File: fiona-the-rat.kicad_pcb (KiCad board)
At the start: 2 copper layers, 83.3 x 89.9 mm, 104 parts, among them J1 USB_TP_P, J10 ~{CHG}_TP, J11 +1V1_TP, J12 VBAT_TP, J13 +3V3_TP, J14 SWD, J15 BMS_COUT_TP, J16 BMS_DOUT_TP, J17 BAT_P_JMP, J18 BAT_N_JMP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

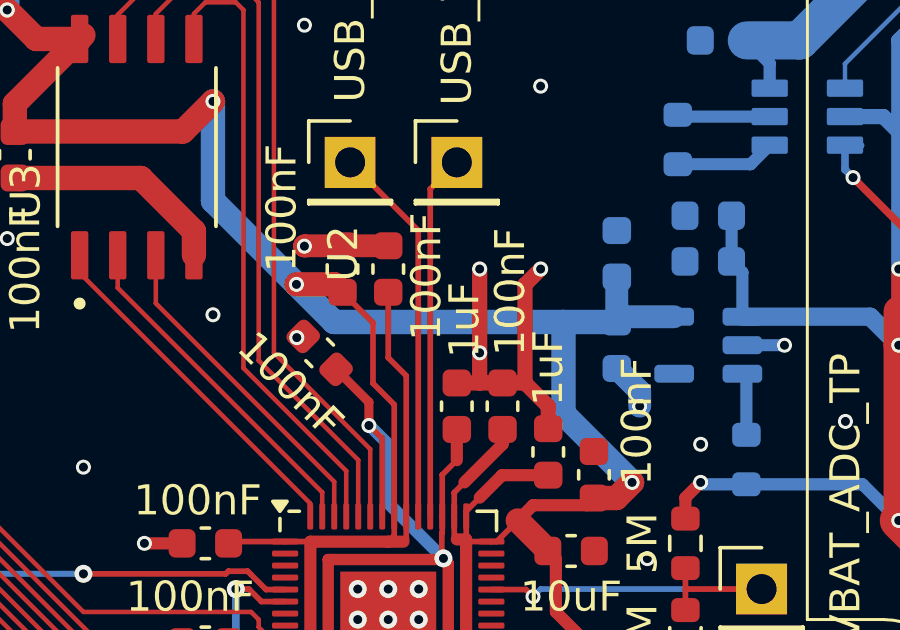
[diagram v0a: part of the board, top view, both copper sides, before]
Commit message: swap 3v3 caps on rp2040
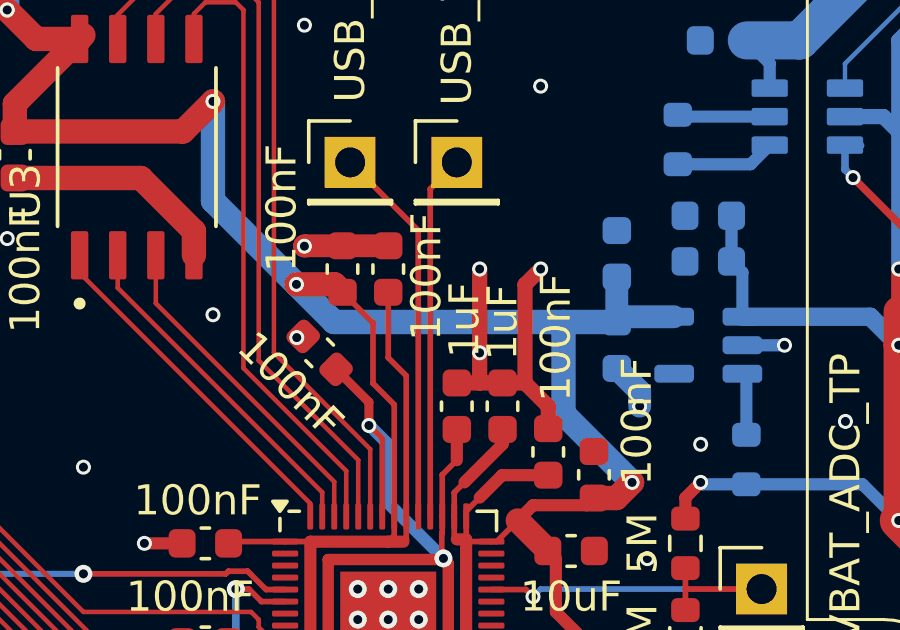
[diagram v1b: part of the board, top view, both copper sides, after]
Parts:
- moved C11 2.16 mm to (143.5, 94.5)
- moved C22 2.16 mm to (145.0, 96.0)
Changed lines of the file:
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@@
 	(footprint "Capacitor_SMD:C_0603_1608Metric"
 		(layer "F.Cu")
-		(at 143.51 94.488 90)
+		(at 145.034 96.012 90)
 		(descr "Capacitor SMD 0603 (1608 Metric), square (rectangular) end terminal, IPC-7351 nominal, (Body size source: IPC-SM-782 page 76, https://www.pcb-3d.com/wordpress/wp-content/uploads/ipc-sm-782a_amendment_1_and_2.pdf), generated with kicad-footprint-generator")
 		(tags "capacitor")
@@
 		(at 139.7 88.9 90)
 		(property "Reference" "U2"
-			(at -0.5 -1.5 90)
+			(at 0.008 3.072 90)
 			(unlocked yes)
 			(layer "F.SilkS")
+			(hide yes)
 			(effects
 				(font
@@
 			(layer "F.SilkS")
 		)
-		(fp_text user "${REFERENCE}"
-			(at -0.5 1.5 90)
-			(unlocked yes)
-			(layer "F.Fab")
-			(effects
-				(font
-					(size 1 1)
-					(thickness 0.15)
-				)
-			)
-		)
 		(pad "1" thru_hole circle
 			(at 15.237545 -12.7 90)
@@
 				"a2ccb8ad-579d-4426-9feb-ad976e31a146" "a3a729a7-c3e8-4f9c-9854-a2e688bbd4e9"
 				"acdef2fa-4fc8-4049-8d66-e1936bda30b8" "ce06db57-7f60-4f2b-af29-020d9ed6190e"
-				"ce06db57-7f60-4f2b-af29-020d9ed6190e" "ce06db57-7f60-4f2b-af29-020d9ed6190e"
-				"ce06db57-7f60-4f2b-af29-020d9ed6190e" "ce18d080-f9fe-4c4e-bd94-48005d2792bd"
-				"d182e725-c283-4e68-ab7d-6e44680550b5" "e2b29b8d-fd9e-490c-9fd3-35cf895c7c33"
-				"f8c461c9-510e-430b-a64b-ff15fdf24184"
+				"ce18d080-f9fe-4c4e-bd94-48005d2792bd" "d182e725-c283-4e68-ab7d-6e44680550b5"
+				"e2b29b8d-fd9e-490c-9fd3-35cf895c7c33" "f8c461c9-510e-430b-a64b-ff15fdf24184"
 			)
 		)
@@
 	(footprint "Capacitor_SMD:C_0603_1608Metric"
 		(layer "F.Cu")
-		(at 145.034 96.012 90)
+		(at 143.51 94.488 90)
 		(descr "Capacitor SMD 0603 (1608 Metric), square (rectangular) end terminal, IPC-7351 nominal, (Body size source: IPC-SM-782 page 76, https://www.pcb-3d.com/wordpress/wp-content/uploads/ipc-sm-782a_amendment_1_and_2.pdf), generated with kicad-footprint-generator")
 		(tags "capacitor")
@@
 	)
 	(segment
-		(start 142.3 97.984)
-		(end 142.748 97.536)
-		(width 0.1905)
-		(layer "F.Cu")
-		(net 3)
-	)
-	(segment
 		(start 137.1 99)
 		(end 137.1042 99.0042)
@@
 	)
 	(segment
+		(start 142.3 98.9238)
+		(end 142.2958 98.928)
+		(width 0.1905)
+		(layer "F.Cu")
+		(net 3)
+	)
+	(segment
 		(start 128.765 70.117)
 		(end 128.765 70.104)
@@
 	)
 	(segment
-		(start 142.3 98.1625)
-		(end 142.3 98.9238)
-		(width 0.1905)
-		(layer "F.Cu")
-		(net 3)
-	)
-	(segment
 		(start 127.967 82.247)
 		(end 127 81.28)
@@
 	)
 	(segment
-		(start 142.3 98.1625)
-		(end 142.3 97.984)
-		(width 0.1905)
-		(layer "F.Cu")
-		(net 3)
-	)
-	(segment
 		(start 140.3 98.1625)
 		(end 140.3 93.472)
@@
 	)
 	(segment
-		(start 142.3 98.9238)
-		(end 142.2958 98.928)
-		(width 0.1905)
-		(layer "F.Cu")
-		(net 3)
-	)
-	(segment
 		(start 127.254 85.331)
 		(end 127.254 84.406)
@@
 	)
 	(segment
+		(start 142.3 97.984)
+		(end 142.748 97.536)
+		(width 0.1905)
+		(layer "F.Cu")
+		(net 3)
+	)
+	(segment
+		(start 142.3 98.1625)
+		(end 142.3 97.984)
+		(width 0.1905)
+		(layer "F.Cu")
+		(net 3)
+	)
+	(segment
 		(start 139.970042 104.394)
 		(end 140.092042 104.272)
@@
 		(layer "F.Cu")
 		(net 3)
+	)
+	(segment
+		(start 142.3 98.1625)
+		(end 142.3 98.9238)
+		(width 0.1905)
+		(layer "F.Cu")
+		(net 3)

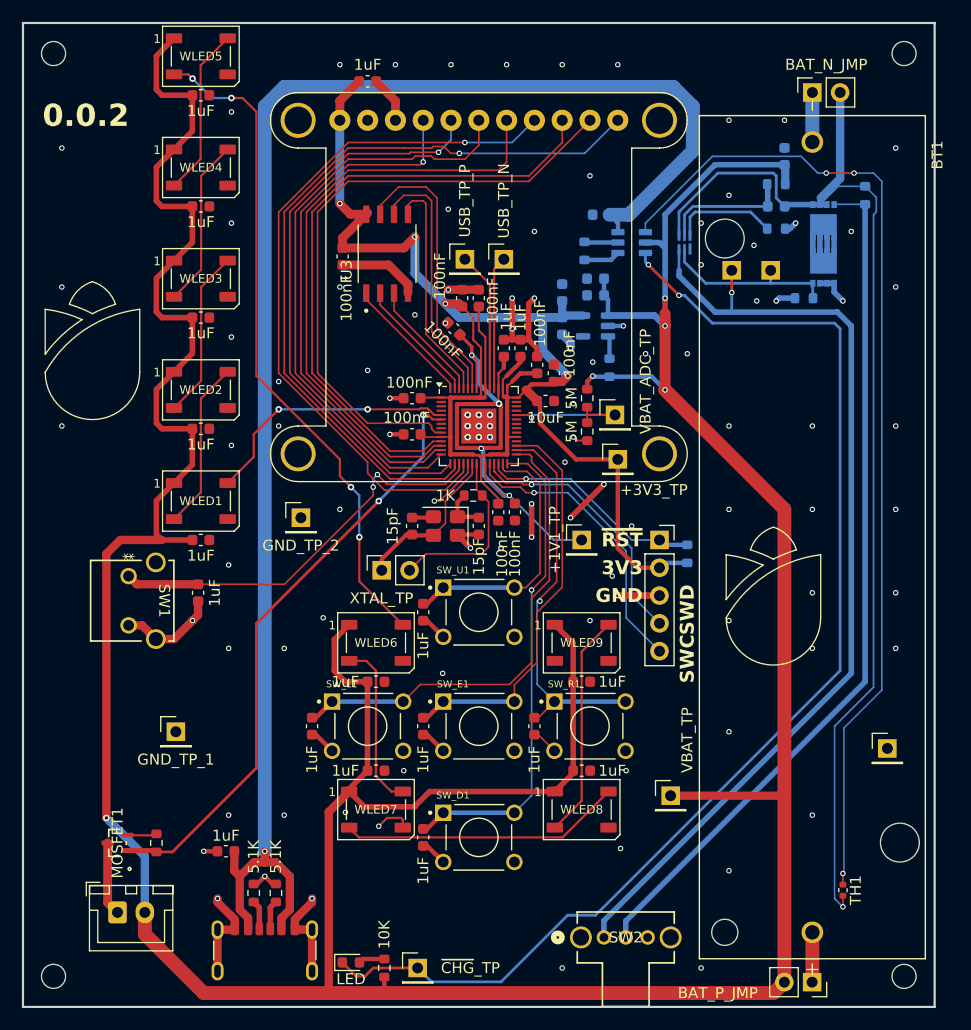
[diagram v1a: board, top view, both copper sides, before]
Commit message: breakout GPIO[0..=2]
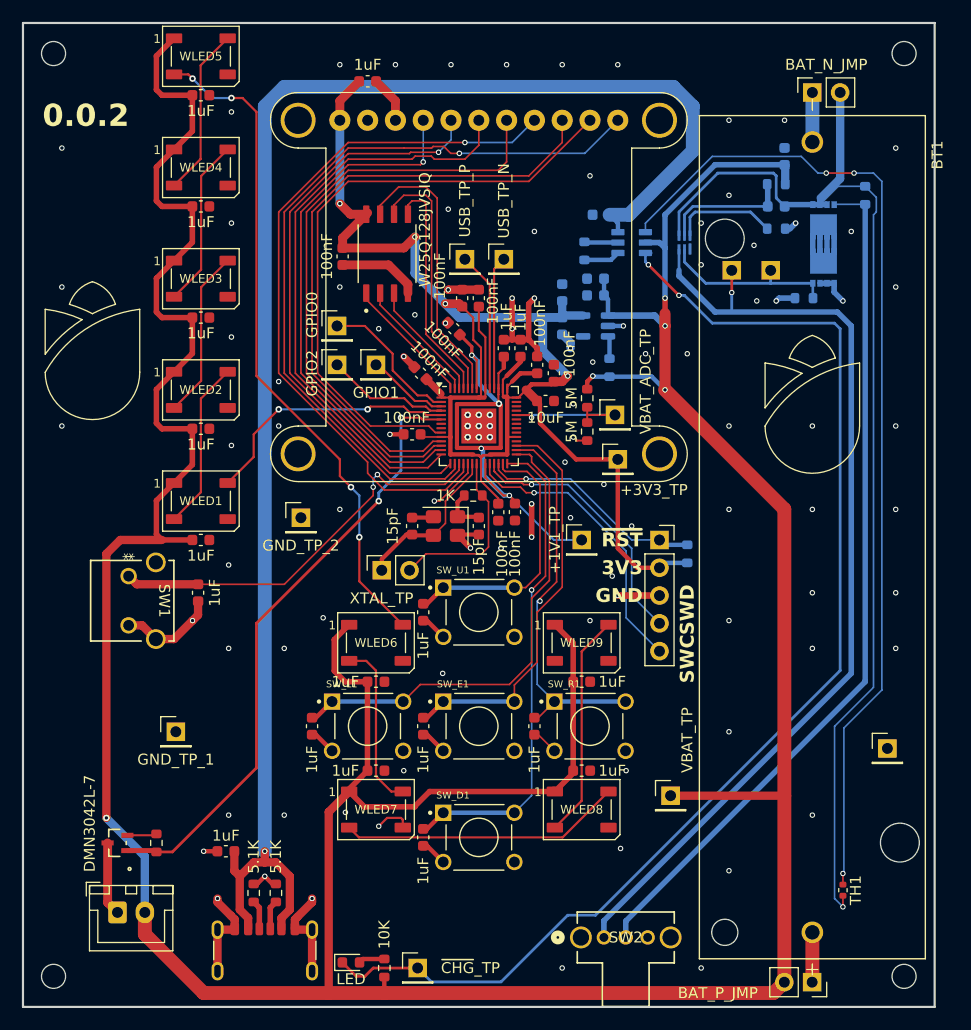
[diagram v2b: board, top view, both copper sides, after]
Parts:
- added J19: GPIO0, Connector_PinHeader_2.54mm:PinHeader_1x01_P2.54mm_Vertical, F.Cu at (126.7, 92.5)
- added J20: GPIO1, Connector_PinHeader_2.54mm:PinHeader_1x01_P2.54mm_Vertical, F.Cu at (130.3, 96.0)
- added J21: GPIO2, Connector_PinHeader_2.54mm:PinHeader_1x01_P2.54mm_Vertical, F.Cu at (126.7, 96.0)
- moved C23 2.41 mm to (134.4, 96.8), turned to 135 degrees
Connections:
- U1 pad 2: unconnected-(U1-GPIO0-Pad2) -> Net-(J19-Pin_1)
- U1 pad 3: unconnected-(U1-GPIO1-Pad3) -> Net-(J20-Pin_1)
- U1 pad 4: unconnected-(U1-GPIO2-Pad4) -> Net-(J21-Pin_1)
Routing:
- net Net-(J19-Pin_1): track 0.00 -> 13.3 mm
- net Net-(J21-Pin_1): track 0.00 -> 11.6 mm
- net Net-(J20-Pin_1): track 0.00 -> 7.53 mm
- net GND: track 125.7 -> 121.5 mm
- net Net-(MOSFET1-G): track 55.4 -> 56.2 mm

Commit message: add haptic motor
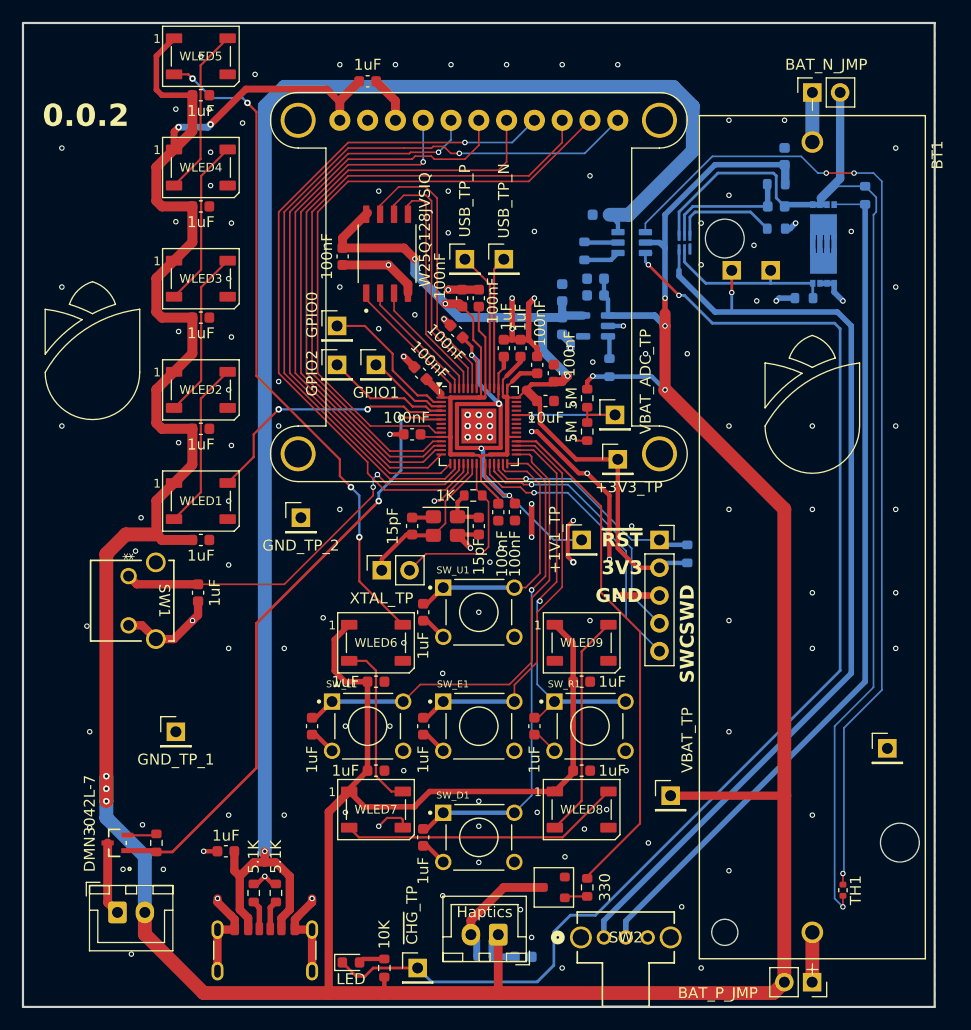
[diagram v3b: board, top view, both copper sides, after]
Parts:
- removed REF** (x4): MountingHole_2.2mm_M2, MountingHole:MountingHole_2.2mm_M2
- added C40: 10uF, Capacitor_SMD:C_0603_1608Metric, B.Cu at (143.8, 150.1)
- added D2: 1N4148WT, Diode_SMD:D_SOD-523, B.Cu at (140.2, 150.1)
- added J22: Haptics, Connector_JST:JST_XH_B2B-XH-A_1x02_P2.50mm_Vertical, F.Cu at (141.5, 148.1)
- added Q1: MMBT2222A, PCM_Package_TO_SOT_SMD_AKL:SOT-23, F.Cu at (146.6, 143.8)
- added R15: 330, Resistor_SMD:R_0603_1608Metric, F.Cu at (149.6, 143.8)
- moved C8 0.36 mm to (137.7, 93.0)
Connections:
- C2 pad 1: +3V3 -> VBAT
- U1 pad 32: unconnected-(U1-GPIO21-Pad32) -> Net-(U1-GPIO21)
- U2 pad 1: +3V3 -> VBAT
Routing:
- net Net-(U1-GPIO21): track 0.00 -> 47.7 mm
- net VBAT: track 365.5 -> 402.0 mm, vias 5 -> 9
- net GND: track 121.5 -> 141.7 mm, vias 103 -> 144
- net +3V3: track 147.3 -> 130.6 mm, vias 4 -> 3
- net Net-(D2-A): track 0.00 -> 11.4 mm
- net Net-(Q1-B): track 0.00 -> 2.10 mm
- net ~{CHG}: track 111.0 -> 112.8 mm

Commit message: Flipped display pin ordering
:/
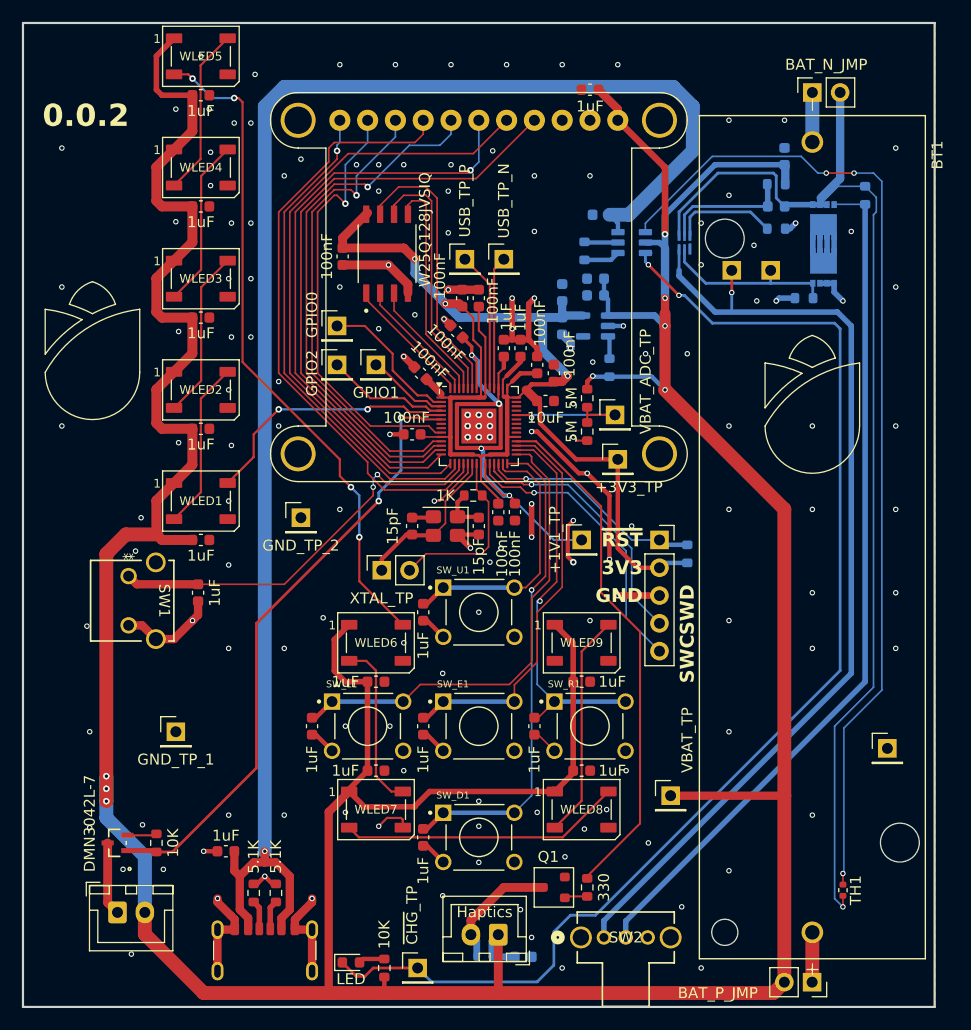
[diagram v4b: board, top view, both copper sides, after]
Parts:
- moved C2 20.3 mm to (149.9, 70.9), turned to 180 degrees
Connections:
- U2 pad 1: VBAT -> BACKLIGHT
- U2 pad 10: SD_CS -> unconnected-(U2-+3V3-Pad10)
- U2 pad 11: BACKLIGHT -> VBAT
- U2 pad 2: unconnected-(U2-+3V3-Pad2) -> SD_CS
- U2 pad 3: GND -> LCD_DCX
- U2 pad 4: LCD_CLK -> LCD_RST
- U2 pad 5: LCD_MISO -> LCD_CS
- U2 pad 7: LCD_CS -> LCD_MISO
- U2 pad 8: LCD_RST -> LCD_CLK
- U2 pad 9: LCD_DCX -> GND
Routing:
- net BACKLIGHT: track 69.7 -> 45.7 mm
- net SD_CS: track 56.6 -> 40.2 mm, vias 0 -> 1
- net LCD_DCX: track 57.4 -> 43.3 mm, vias 0 -> 1
- net VBAT: track 402.0 -> 392.9 mm, vias 9 -> 8
- net LCD_RST: track 64.9 -> 56.2 mm, vias 1 -> 0
- net LCD_CLK: track 48.3 -> 56.2 mm, vias 1 -> 0
- net LCD_CS: track 54.6 -> 48.2 mm, vias 0 -> 1
- net GND: track 141.7 -> 137.4 mm, vias 144 -> 156
- net LCD_MISO: track 52.8 -> 56.8 mm, vias 1 -> 0
- net LCD_MOSI: track 53.9 -> 54.6 mm, vias 0 -> 1

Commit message: DRC fixes, swapped cryst lib
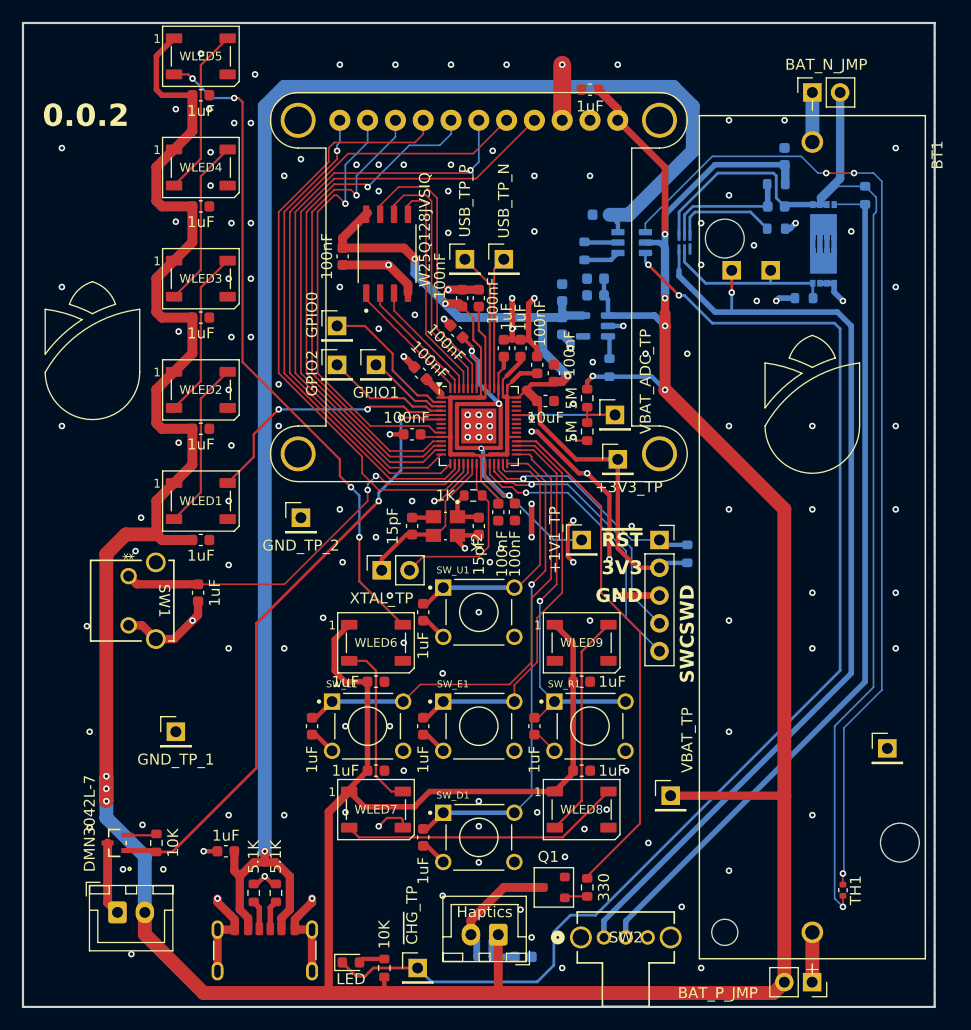
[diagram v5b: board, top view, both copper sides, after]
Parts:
- removed Y1: Crystal_GND24, Crystal:Crystal_SMD_Abracon_ABM8G-4Pin_3.2x2.5mm
- added Y2: ABM8G-12.000MHZ-18-D2Y-T, pfornage-kicad-lib:XTAL_ABM8G-12.000MHZ-18-D2Y-T, F.Cu at (136.7, 110.7)
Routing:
- net GND: track 137.4 -> 142.3 mm, vias 156 -> 160
